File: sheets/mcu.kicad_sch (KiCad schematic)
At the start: 37 parts, among them SW1 SW_Nidec_CAS-120A1, SW2 SW_Push, U1 STM32H755ZIT6, Y1 25M, Y2 32k768

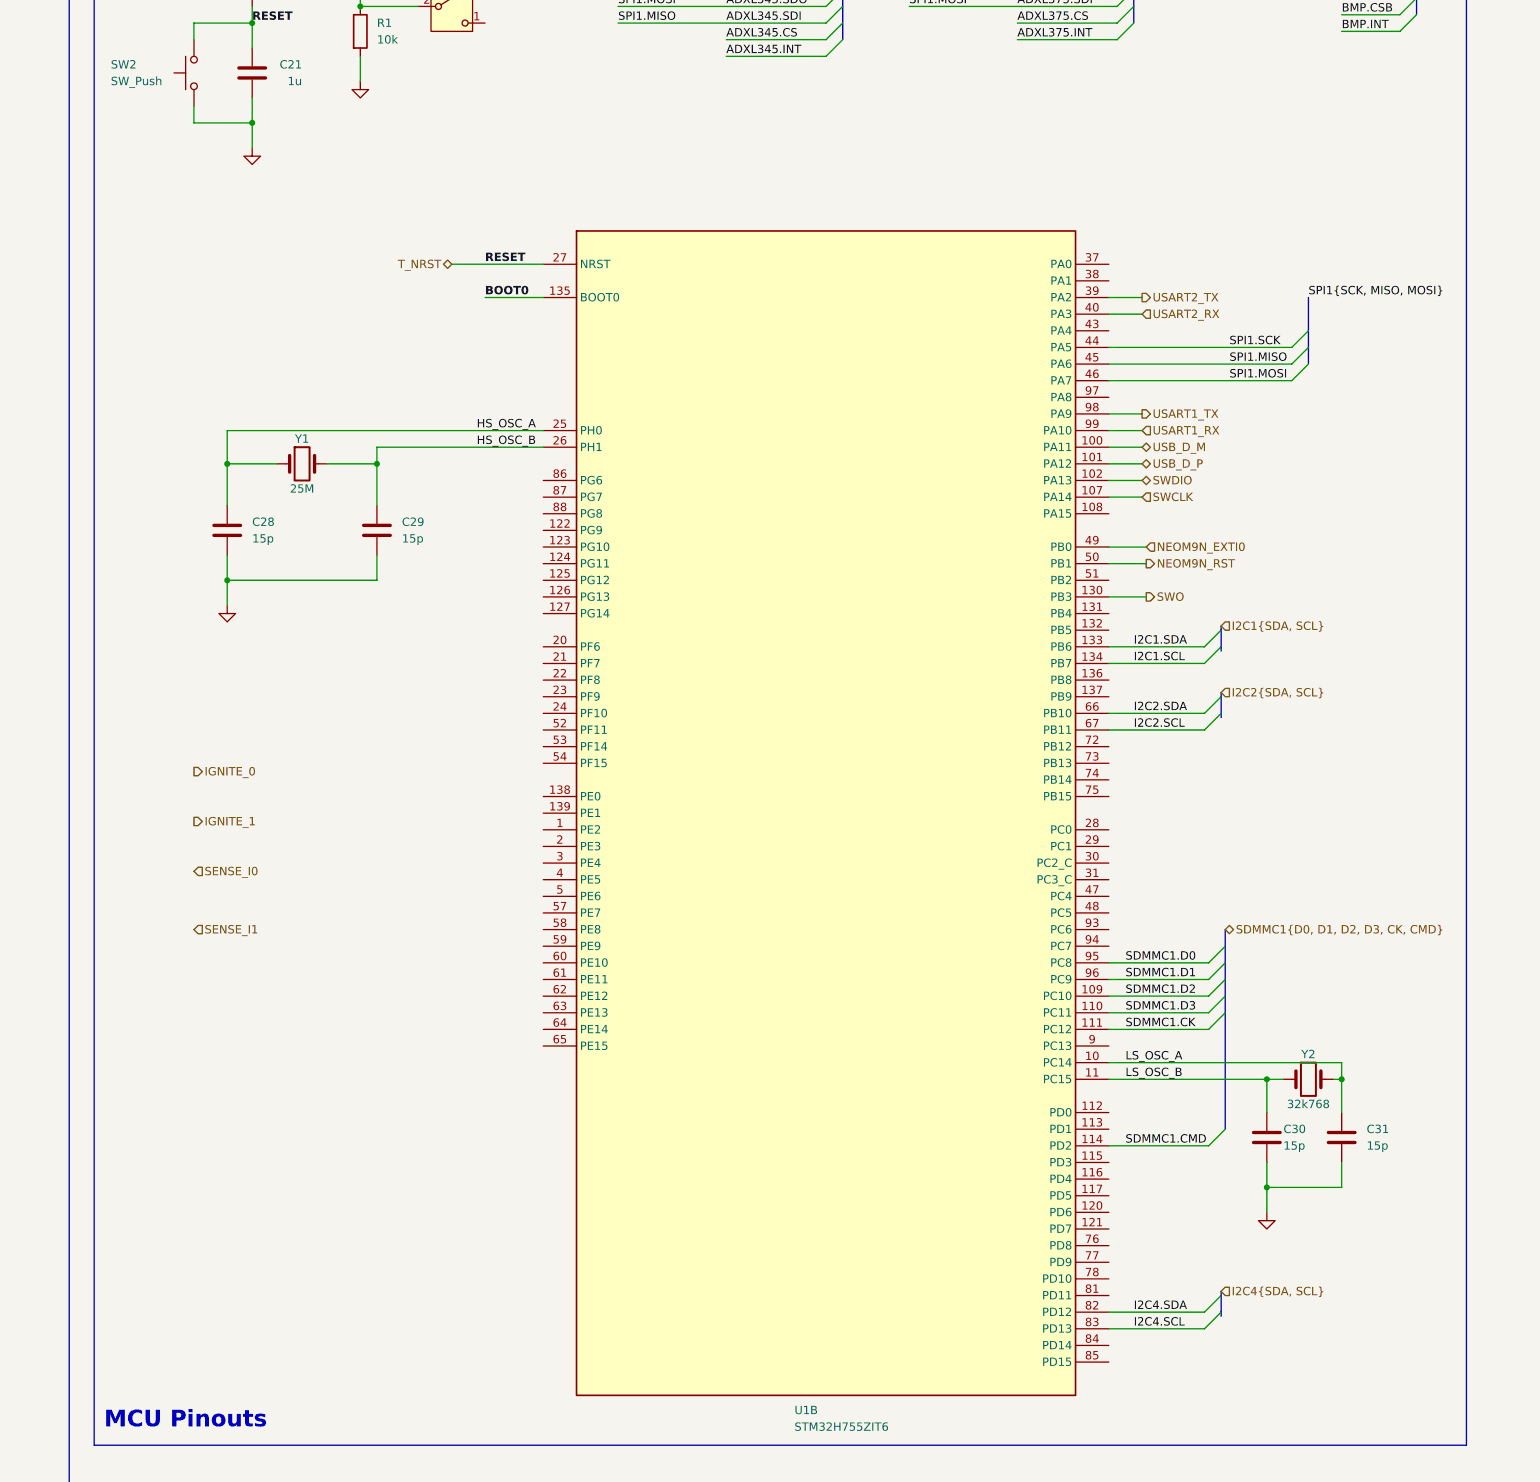
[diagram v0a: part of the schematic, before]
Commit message: removed fd can
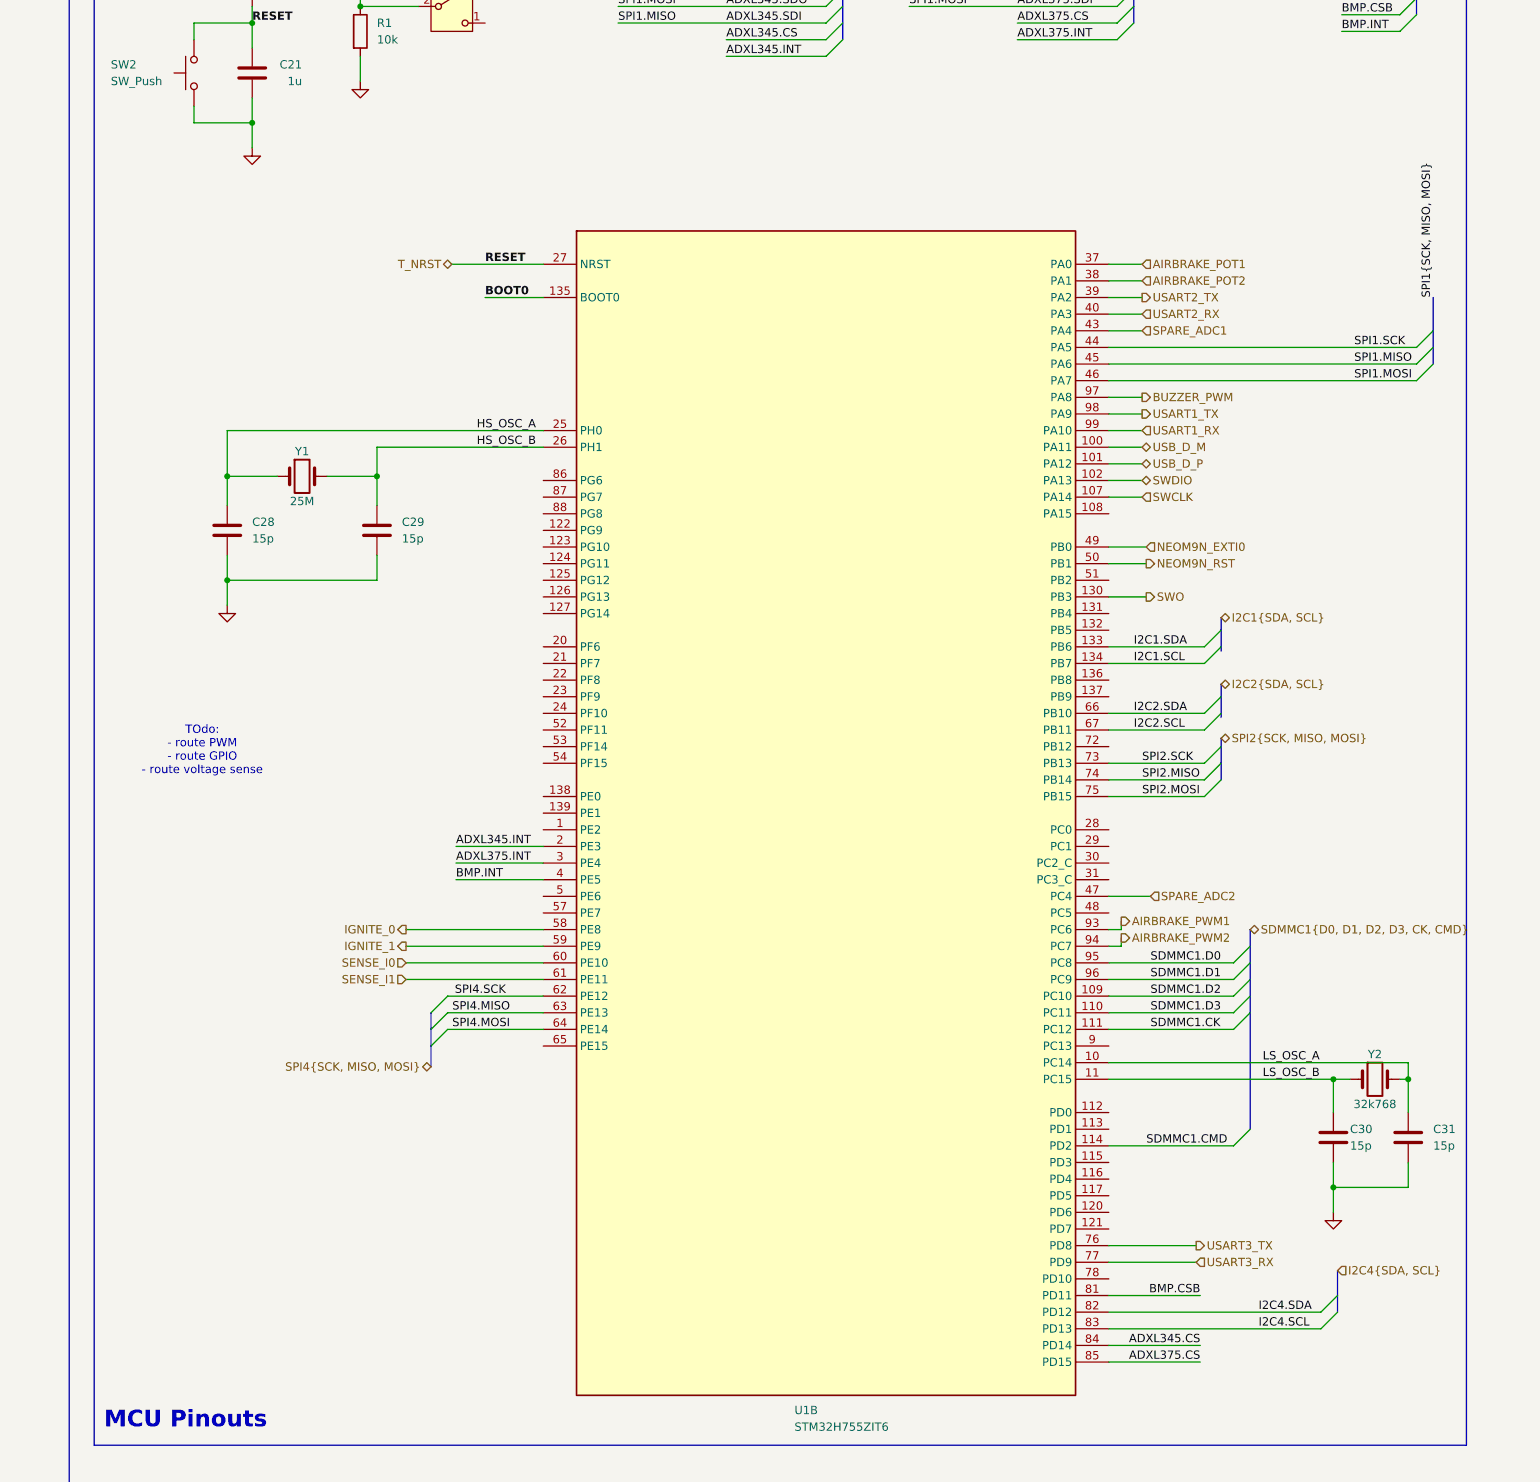
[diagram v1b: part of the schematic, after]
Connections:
- net ADXL345.CS: now also U1.84 (PD14)
- net ADXL345.INT: now also U1.2 (PE3)
- net ADXL375.CS: now also U1.85 (PD15)
- net ADXL375.INT: now also U1.3 (PE4)
- net BMP.CSB: now also U1.81 (PD11)
- net BMP.INT: now also U1.4 (PE5)
- net IGNITE_0: now also U1.58 (PE8)
- net IGNITE_1: now also U1.59 (PE9)
- net SENSE_I0: now also U1.60 (PE10)
- net SENSE_I1: now also U1.61 (PE11)
- net AIRBRAKE_POT1: now reaches U1.37 (PA0)
- net AIRBRAKE_POT2: now reaches U1.38 (PA1)
- net SPARE_ADC1: now reaches U1.43 (PA4)
- net SPARE_ADC2: now reaches U1.47 (PC4)
- net SPI4.SCK: now reaches U1.62 (PE12)
- net SPI4.MISO: now reaches U1.63 (PE13)
- net SPI4.MOSI: now reaches U1.64 (PE14)
- net SPI2.SCK: now reaches U1.73 (PB13)
- net SPI2.MISO: now reaches U1.74 (PB14)
- net SPI2.MOSI: now reaches U1.75 (PB15)
- net USART3_TX: now reaches U1.76 (PD8)
- net USART3_RX: now reaches U1.77 (PD9)
- net AIRBRAKE_PWM1: now reaches U1.93 (PC6)
- net AIRBRAKE_PWM2: now reaches U1.94 (PC7)
- net BUZZER_PWM: now reaches U1.97 (PA8)
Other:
- note added: "TOdo: - route PWM - route GPIO - route voltage sense"
- moved on the sheet: C30, C31, Y1, Y2

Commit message: added spi
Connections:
- net +3V3: no longer U1.90 (VDD50_USB)
- new net +5V: U1.90 (VDD50_USB)
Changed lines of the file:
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@@
 	)
 	(junction
-		(at 119.38 82.55)
-		(diameter 0)
-		(color 0 0 0 0)
-	)
-	(junction
 		(at 220.98 34.29)
 		(diameter 0)
@@
 	(wire
 		(pts
+			(xy 121.92 79.375) (xy 121.92 86.36)
+		)
+		(stroke
+			(width 0)
+			(type default)
+		)
+	)
+	(wire
+		(pts
 			(xy 386.08 195.58) (xy 388.62 195.58)
 		)
@@
 	(wire
 		(pts
-			(xy 119.38 82.55) (xy 121.92 82.55)
-		)
-		(stroke
-			(width 0)
-			(type default)
-		)
-	)
-	(wire
-		(pts
 			(xy 386.08 195.58) (xy 386.08 200.66)
 		)
@@
 	(wire
 		(pts
-			(xy 121.92 82.55) (xy 121.92 86.36)
-		)
-		(stroke
-			(width 0)
-			(type default)
-		)
-	)
-	(wire
-		(pts
 			(xy 54.61 85.09) (xy 54.61 96.52)
 		)
@@
 					(unit 1)
 				)
+			)
+		)
+	)
+	(symbol
+		(lib_id "power:+5V")
+		(at 121.92 79.375 0)
+		(unit 1)
+		(exclude_from_sim no)
+		(in_bom yes)
+		(on_board yes)
+		(dnp no)
+		(fields_autoplaced yes)
+		(property "Reference" "#PWR0112"
+			(at 121.92 83.185 0)
+			(effects
+				(font
+					(size 1.27 1.27)
+				)
+				(hide yes)
+			)
+		)
+		(property "Value" "+5V"
+			(at 121.92 74.93 0)
+			(effects
+				(font
+					(size 1.27 1.27)
+				)
+			)
+		)
+		(property "Footprint" ""
+			(at 121.92 79.375 0)
+			(effects
+				(font
+					(size 1.27 1.27)
+				)
+				(hide yes)
+			)
+		)
+		(property "Datasheet" ""
+			(at 121.92 79.375 0)
+			(effects
+				(font
+					(size 1.27 1.27)
+				)
+				(hide yes)
+			)
+		)
+		(property "Description" "Power symbol creates a global label with name \"+5V\""
+			(at 121.92 79.375 0)
+			(effects
+				(font
+					(size 1.27 1.27)
+				)
+				(hide yes)
+			)
+		)
+		(pin "1"
+		)
+		(instances
+			(project ""
+				(path "/3f5bc5ea-feaa-4ed9-b0e0-c918b1fb5754/ab6692e5-8cdb-4044-acef-dc950a39c5fc"
+					(reference "#PWR0112")
+					(unit 1)
+				)

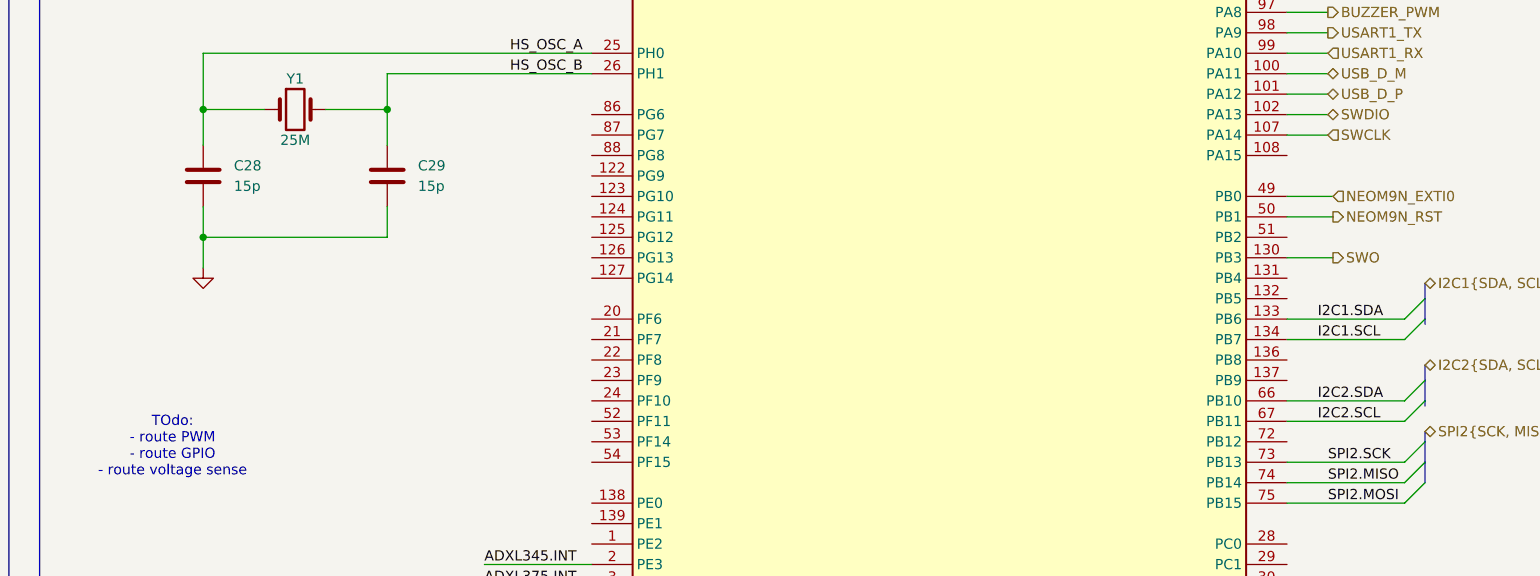
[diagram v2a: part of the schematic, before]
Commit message: led pwm
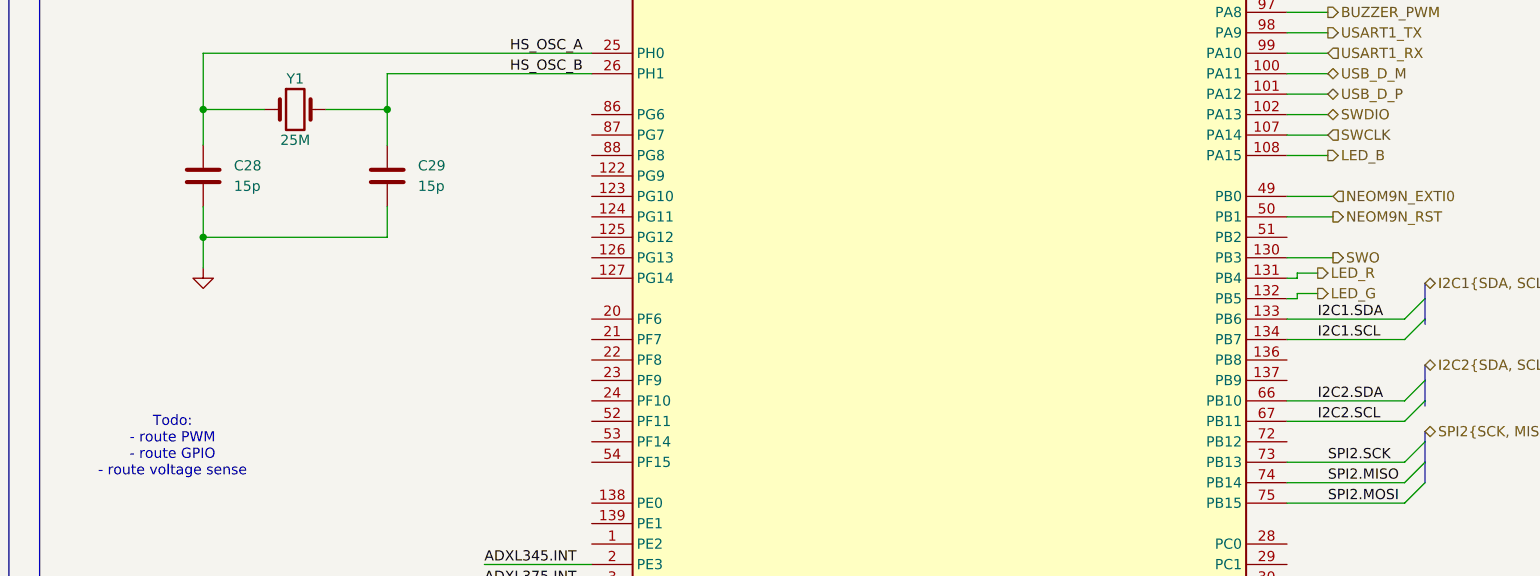
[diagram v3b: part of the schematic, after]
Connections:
- net LED_B: now reaches U1.108 (PA15)
- net LED_R: now reaches U1.131 (PB4)
- net LED_G: now reaches U1.132 (PB5)
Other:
- note added: "Todo: - route PWM - route GPIO - route voltage sense"
- note removed: "TOdo: - route PWM - route GPIO - route voltage sense"
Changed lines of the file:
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@@
 		)
 	)
-	(text "TOdo:\n- route PWM\n- route GPIO\n- route voltage sense\n"
+	(text "Todo:\n- route PWM\n- route GPIO\n- route voltage sense\n"
 		(exclude_from_sim no)
 		(at 213.36 145.415 0)
@@
 	(wire
 		(pts
+			(xy 353.06 124.46) (xy 351.79 124.46)
+		)
+		(stroke
+			(width 0)
+			(type default)
+		)
+	)
+	(wire
+		(pts
 			(xy 220.98 34.29) (xy 220.98 31.75)
 		)
@@
 	(wire
 		(pts
+			(xy 353.06 126.365) (xy 355.6 126.365)
+		)
+		(stroke
+			(width 0)
+			(type default)
+		)
+	)
+	(wire
+		(pts
 			(xy 217.17 103.505) (xy 224.79 103.505)
 		)
@@
 	(wire
 		(pts
+			(xy 353.06 123.825) (xy 353.06 124.46)
+		)
+		(stroke
+			(width 0)
+			(type default)
+		)
+	)
+	(wire
+		(pts
 			(xy 386.08 195.58) (xy 386.08 200.66)
 		)
@@
 	(wire
 		(pts
+			(xy 351.79 109.22) (xy 356.87 109.22)
+		)
+		(stroke
+			(width 0)
+			(type default)
+		)
+	)
+	(wire
+		(pts
 			(xy 266.7 24.13) (xy 266.7 29.21)
 		)
@@
 	(wire
 		(pts
+			(xy 351.79 127) (xy 353.06 127)
+		)
+		(stroke
+			(width 0)
+			(type default)
+		)
+	)
+	(wire
+		(pts
 			(xy 157.48 92.71) (xy 157.48 93.98)
 		)
@@
 	(wire
 		(pts
+			(xy 353.06 127) (xy 353.06 126.365)
+		)
+		(stroke
+			(width 0)
+			(type default)
+		)
+	)
+	(wire
+		(pts
+			(xy 353.06 123.825) (xy 355.6 123.825)
+		)
+		(stroke
+			(width 0)
+			(type default)
+		)
+	)
+	(wire
+		(pts
 			(xy 337.82 36.83) (xy 353.06 36.83)
 		)
@@
 		)
 	)
+	(hierarchical_label "LED_G"
+		(shape output)
+		(at 355.6 126.365 0)
+		(effects
+			(font
+				(size 1.27 1.27)
+			)
+			(justify left)
+		)
+	)
 	(hierarchical_label "SPI2{SCK, MISO, MOSI}"
 		(shape bidirectional)
@@
 		)
 	)
+	(hierarchical_label "LED_B"
+		(shape output)
+		(at 356.87 109.22 0)
+		(effects
+			(font
+				(size 1.27 1.27)
+			)
+			(justify left)
+		)
+	)
 	(hierarchical_label "IGNITE_1"
 		(shape output)
@@
 		)
 	)
+	(hierarchical_label "LED_R"
+		(shape output)
+		(at 355.6 123.825 0)
+		(effects
+			(font
+				(size 1.27 1.27)
+			)
+			(justify left)
+		)
+	)
